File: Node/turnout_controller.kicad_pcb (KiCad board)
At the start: 2 copper layers, 22.4 x 18 mm, 12 parts, among them IC1 L79L05ACD13TR_LDO, IC2 CharliPlexLED-4pin, IC3 ATTINY841-SSU, Q1 NPN, U1 SERVO_CONN_3pin, U2 SPI_PORT_6pin, U3 Detector_conn_4pin

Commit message: changed links
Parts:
- added R1: R, Resistors_SMD:R_0402, F.Cu at (137.4, 37.3)
- added R2: R, Resistors_SMD:R_0402, F.Cu at (138.7, 37.3)
- added R3: R, Resistors_SMD:R_0402, F.Cu at (140.0, 37.3)
- added R4: R, Resistors_SMD:R_0402, F.Cu at (141.2, 37.3)
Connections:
- IC2 pad 1: CP1 -> Net-(IC2-Pad1)
- IC2 pad 2: CP2 -> Net-(IC2-Pad2)
- IC2 pad 3: CP3 -> Net-(IC2-Pad3)
- IC2 pad 4: CP4 -> Net-(IC2-Pad4)
- U1 pad 1: SERVO_POSITIVE -> SERVO_SIGNAL
- U1 pad 2: SERVO_SIGNAL -> SERVO_POSITIVE
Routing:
- net Net-(IC2-Pad4): track 0.00 -> 8.31 mm
- net Net-(IC2-Pad3): track 0.00 -> 8.31 mm
- net Net-(IC2-Pad2): track 0.00 -> 8.31 mm
- net Net-(IC2-Pad1): track 0.00 -> 8.31 mm
- net CP2: track 12.9 -> 7.81 mm, vias 0 -> 2
- net CP1: track 14.7 -> 9.88 mm
- net CP4: track 15.4 -> 11.4 mm, vias 1 -> 2
- net CP3: track 16.5 -> 14.8 mm
- net SERVO_SIGNAL: track 9.42 -> 10.9 mm, vias 0 -> 1
- net SERVO_POSITIVE: track 3.28 -> 4.49 mm
- net A0: track 5.29 -> 4.47 mm
- net A1: track 6.76 -> 6.19 mm
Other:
- board size 22.4 x 18 mm -> 22.4 x 18.4 mm
- board text added: "AMRR node"
- board text added: "S + GND"
- board text added: "version 0.1"
- board text removed: "+ S GND"

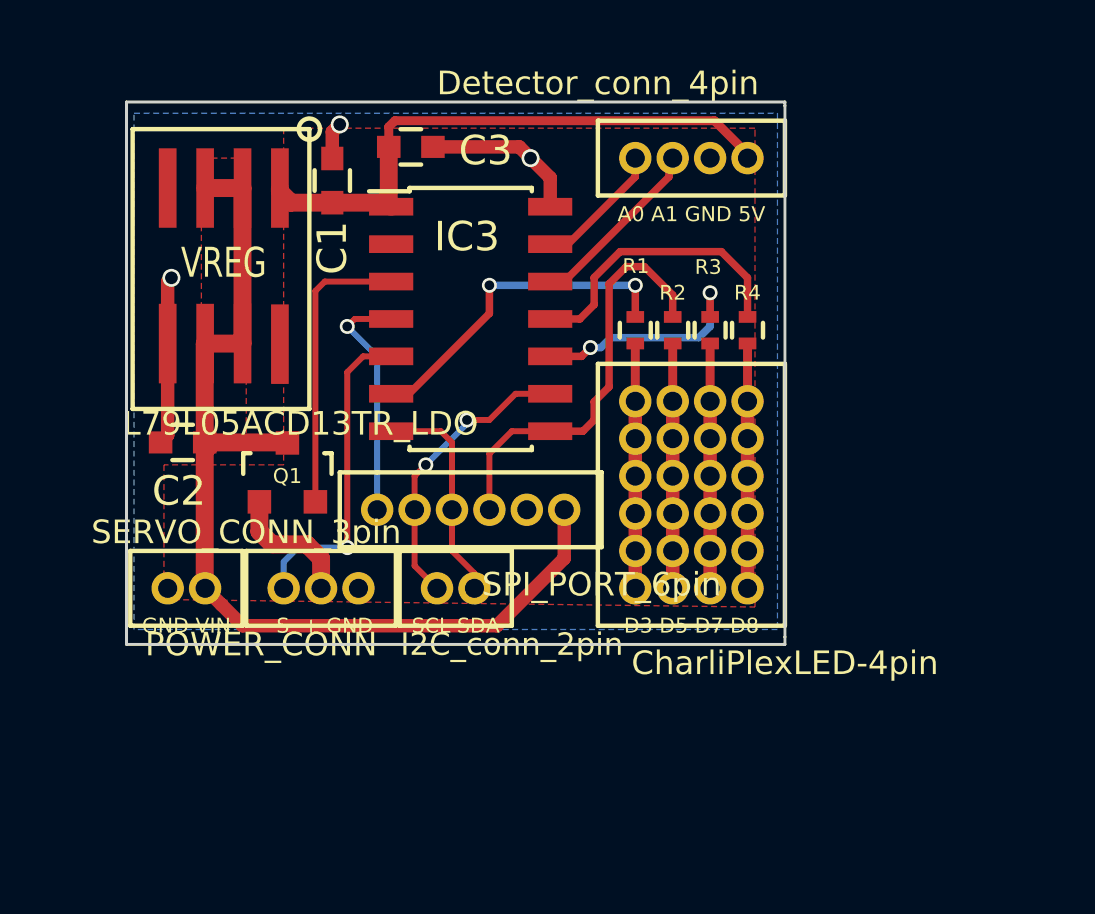
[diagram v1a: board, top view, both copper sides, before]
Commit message: version 0.2 - added extra footprint so that the node can serve as a relay. fixed the servo footprint.
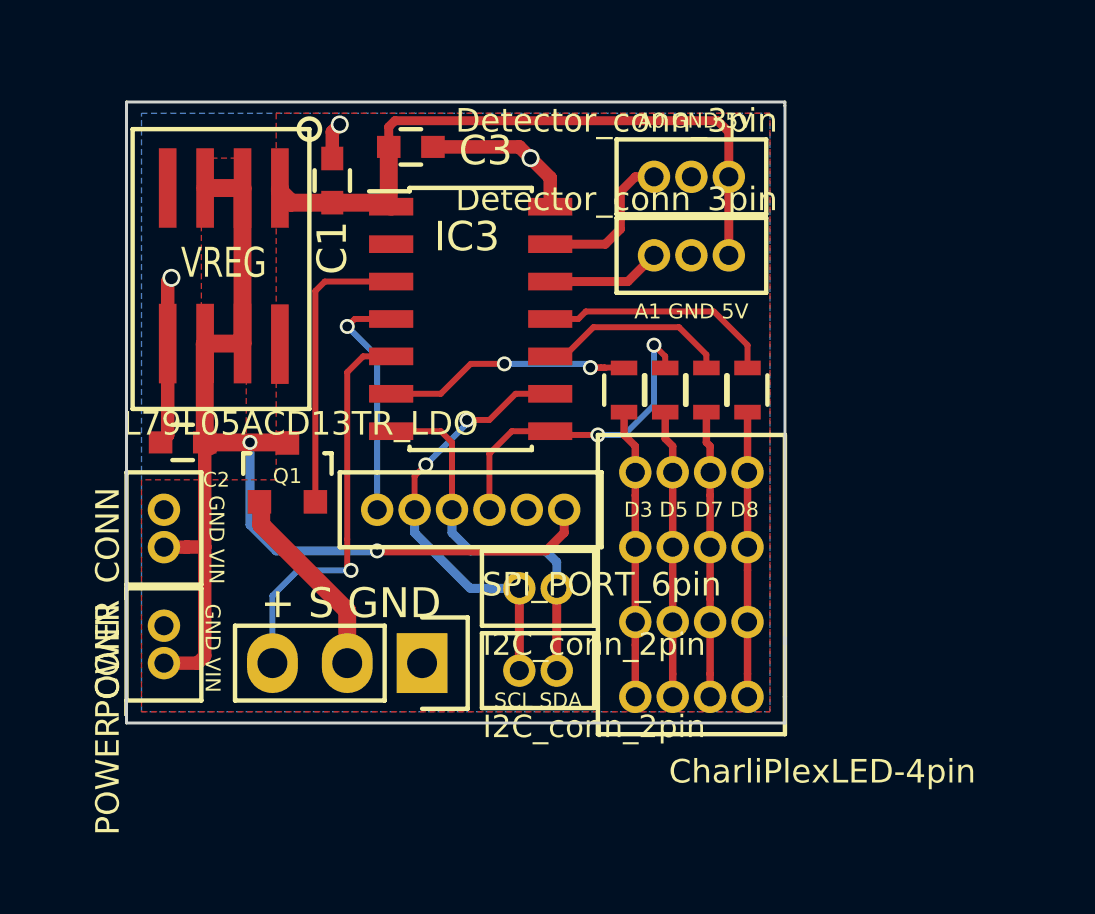
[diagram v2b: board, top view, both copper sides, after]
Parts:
- added U4: Detector_conn_3pin, custom_footprints:block_3pin_corrected, F.Cu at (139.3, 32.1)
- added conn3: I2C_conn_2pin, custom_footprints:I2C_conn_2pin, F.Cu at (133.5, 48.9)
- added conn4: POWER_CONN, custom_footprints:PWR_CONN_1.27mm, F.Cu at (121.4, 48.6)
- IC2: footprint custom_footprints:Charliplex_LED_4pin -> custom_footprints:Charliplex_LED_4x4pin
- R1, R2, R3, R4: footprint Resistors_SMD:R_0402 -> Resistors_SMD:R_0603
- U1: footprint custom_footprints:SERVO_CONN_3pin_corrected -> custom_footprints:servo_conn_1x03
- U3: value Detector_conn_4pin -> Detector_conn_3pin; footprint custom_footprints:Detector_conn_4pin -> custom_footprints:block_3pin_corrected
- moved U1 4.27 mm to (130.2, 48.6), turned to 180 degrees
- moved U3 3.30 mm to (139.3, 34.8)
- moved conn1 2.79 mm to (133.5, 46.1)
- moved IC2 2.41 mm to (140.0, 42.2)
- moved R1 2.07 mm to (137.0, 39.4)
- moved R2 2.05 mm to (138.4, 39.4)
- moved R3 2.04 mm to (139.8, 39.4)
- moved R4 2.03 mm to (141.2, 39.4)
- moved conn2 1.98 mm to (121.4, 44.7), turned to 90 degrees
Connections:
- U3 pad 1: A0 -> A1
- U3 pad 2: A1 -> GND
- U3 pad 3: GND -> +5V
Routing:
- net SDA: track 7.49 -> 12.9 mm
- net SCL: track 9.96 -> 14.9 mm
- net VIN: track 34.5 -> 39.2 mm, vias 0 -> 2
- net +5V: track 19.6 -> 22.7 mm
- net CP3: track 14.8 -> 11.7 mm, vias 0 -> 2
- net SERVO_SIGNAL: track 10.9 -> 13.8 mm
- net CP4: track 11.4 -> 8.89 mm
- net A1: track 6.19 -> 3.89 mm
- net SERVO_POSITIVE: track 4.49 -> 6.71 mm
- net CP1: track 9.88 -> 8.05 mm
- net Net-(IC2-Pad4): track 8.31 -> 9.82 mm
- net Net-(IC2-Pad3): track 8.31 -> 9.77 mm
- net Net-(IC2-Pad2): track 8.31 -> 9.72 mm
- net Net-(IC2-Pad1): track 8.31 -> 9.66 mm
- net CP2: track 7.81 -> 6.55 mm, vias 2 -> 0
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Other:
- board size 22.4 x 18.4 mm -> 22.4 x 21.1 mm
- board text added: "+ S GND"
- board text added: "A0 GND 5V"
- board text added: "A1 GND 5V"
- board text added: "version 0.2"
- board text removed: "A0 A1 GND 5V"
- board text removed: "S + GND"
- board text removed: "version 0.1"
